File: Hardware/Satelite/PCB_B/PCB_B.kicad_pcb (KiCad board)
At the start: 2 copper layers, 54 x 54 mm, 92 parts, among them IC1 MCP1642B-50I_MS, IC2 MCP1642B-50I_MS, J1 Conector_PCB_B-C, J2 Conector_PCB_A-B, M1 Spacer, M2 Spacer, M3 Spacer, Q1 SSM3J338R,LF, Q2 SSM3J338R,LF, Q3 SSM3J338R,LF, U1 MIC5353-3.3YMT, U10 BQ21040DBVR, U2 ADP2108AUJ-3.3, U3 INA194, U4 MCP6001-OT, U5 INA194, U6 MCP6001-OT, U7 INA216A4RSWR, U8 BQ27441DRZR-G1A, U9 MCP6001-OT

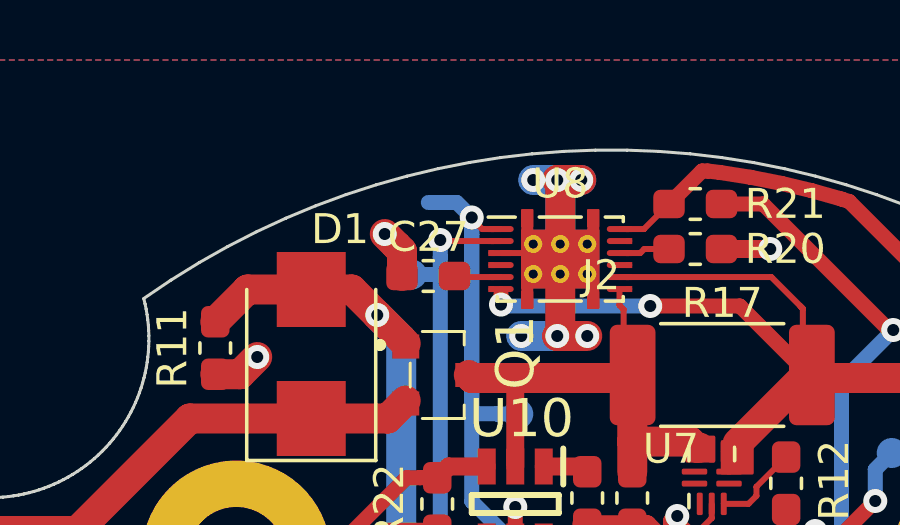
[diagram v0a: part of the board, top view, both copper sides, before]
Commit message: PCB_B plano de masa mejorado
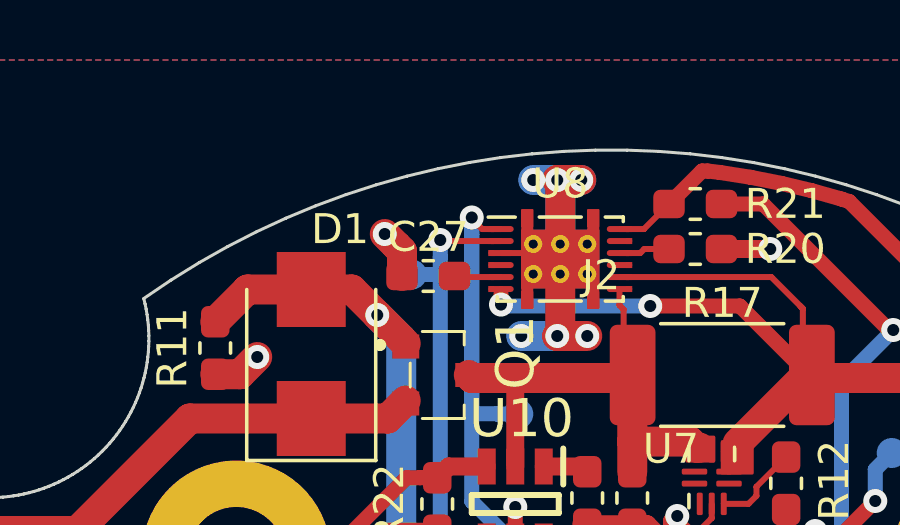
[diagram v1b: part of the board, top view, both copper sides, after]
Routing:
- net /SDA: track 59.2 -> 57.5 mm
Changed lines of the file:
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@@
     (thickness 1.6)
     (drawings 21)
-    (tracks 854)
+    (tracks 852)
     (zones 0)
     (modules 92)
@@
   (segment (start -4.625 13.5964) (end -5.1 13.5964) (width 0.6) (layer B.Cu) (net 3) (status 30))
   (segment (start -5.1 13.5964) (end -6.3 12.3964) (width 0.6) (layer B.Cu) (net 3) (status 10))
+  (segment (start 13.35 -5.205) (end 13.35 -4.73) (width 0.2) (layer F.Cu) (net 3) (status 10))
+  (segment (start 12.599999 -4.399995) (end 12.2 -4.799994) (width 0.2) (layer F.Cu) (net 3))
+  (segment (start 13.019995 -4.399995) (end 12.599999 -4.399995) (width 0.2) (layer F.Cu) (net 3))
+  (segment (start 13.35 -4.73) (end 13.019995 -4.399995) (width 0.2) (layer F.Cu) (net 3))
+  (segment (start 8.200018 -10.8) (end 9.2 -10.8) (width 1) (layer F.Cu) (net 3))
+  (segment (start 7 -10.8) (end 8.200018 -10.8) (width 1) (layer B.Cu) (net 3))
+  (via (at 7.4 -16) (size 0.8) (drill 0.4) (layers F.Cu B.Cu) (net 3))
+  (segment (start 9 -16) (end 7.4 -16) (width 1) (layer B.Cu) (net 3))
+  (via (at 0.11 15.07) (size 0.8) (drill 0.4) (layers F.Cu B.Cu) (net 3))
+  (segment (start 1.3 15.075) (end 0.115 15.075) (width 1) (layer F.Cu) (net 3))
+  (segment (start 0.115 15.075) (end 0.11 15.07) (width 1) (layer F.Cu) (net 3))
+  (segment (start -0.695 14.265) (end 0.11 15.07) (width 1) (layer F.Cu) (net 3))
+  (segment (start -0.695 13.13) (end -0.695 14.265) (width 1) (layer F.Cu) (net 3))
   (segment (start 4.575 -6.45) (end 4.2 -6.075) (width 0.6) (layer F.Cu) (net 4) (status 30))
   (segment (start 5.85 -6.45) (end 4.575 -6.45) (width 0.6) (layer F.Cu) (net 4) (status 30))
@@
   (segment (start -7.81 5.565001) (end -7.825 5.550001) (width 1) (layer F.Cu) (net 5))
   (segment (start -7.81 6.19) (end -7.81 5.565001) (width 1) (layer F.Cu) (net 5))
+  (segment (start 2.67 13.13) (end 2.9 13.36) (width 1) (layer F.Cu) (net 5))
+  (segment (start 1.355 13.13) (end 2.67 13.13) (width 1) (layer F.Cu) (net 5))
+  (segment (start 2.9 12.75) (end 2.9 13.36) (width 1) (layer F.Cu) (net 5))
+  (segment (start 2.9 13.36) (end 2.9 16.2) (width 1) (layer F.Cu) (net 5))
   (segment (start -4.625 11.1964) (end -0.825 11.1964) (width 0.5) (layer B.Cu) (net 6) (status 30))
   (segment (start 18.025 22.925) (end 18.6 22.925) (width 1) (layer F.Cu) (net 6) (status 20))
@@
   (segment (start 11.3 -11.8) (end 6.37251 -11.8) (width 0.5) (layer B.Cu) (net 10))
   (segment (start 16.3875 -9.4) (end 14.212501 -7.225001) (width 1) (layer F.Cu) (net 10) (status 10))
+  (segment (start 13.925 -6.78) (end 13.75 -6.955) (width 0.2) (layer F.Cu) (net 10) (status 20))
+  (segment (start 13.925 -6.28) (end 13.925 -6.78) (width 0.2) (layer F.Cu) (net 10) (status 10))
   (segment (start 23.675 18.8) (end 24.2 18.275) (width 0.5) (layer F.Cu) (net 11) (status 20))
   (segment (start 22.475 18.8) (end 23.675 18.8) (width 0.5) (layer F.Cu) (net 11) (status 10))
@@
   (segment (start -9.2 7.29) (end -9.2 7.855685) (width 0.5) (layer F.Cu) (net 19))
   (segment (start -9.2 7.855685) (end -12.450001 11.105686) (width 0.5) (layer F.Cu) (net 19))
+  (via (at 16.9 -1.07) (size 0.8) (drill 0.4) (layers F.Cu B.Cu) (net 19))
+  (segment (start 16.925 -1.1) (end 16.9 -1.075) (width 0.5) (layer F.Cu) (net 19))
+  (segment (start 19.4 -11) (end 17.675 -9.275) (width 0.5) (layer B.Cu) (net 19))
+  (segment (start 17.299999 -1.469999) (end 16.9 -1.07) (width 0.5) (layer B.Cu) (net 19))
+  (segment (start 17.675 -9.275) (end 17.675 -1.845) (width 0.5) (layer B.Cu) (net 19))
+  (segment (start 17.675 -1.845) (end 17.299999 -1.469999) (width 0.5) (layer B.Cu) (net 19))
+  (segment (start 16.9 -1.075) (end 16.9 -1.07) (width 0.5) (layer F.Cu) (net 19))
+  (segment (start 17.75 -1.1) (end 16.925 -1.1) (width 0.5) (layer F.Cu) (net 19))
+  (segment (start 17.675 -1.025) (end 17.75 -1.1) (width 0.5) (layer F.Cu) (net 19))
+  (segment (start 17.675 2.4) (end 17.675 -1.025) (width 0.5) (layer F.Cu) (net 19))
   (segment (start 27.19001 14.51001) (end 17.152008 14.51001) (width 0.5) (layer F.Cu) (net 20))
   (segment (start 27.95 16.3) (end 27.95 15.27) (width 0.5) (layer F.Cu) (net 20) (status 10))
@@
   (segment (start 11.791998 1.15) (end 5.35 -5.291998) (width 0.5) (layer B.Cu) (net 25))
   (segment (start 21.2 1.15) (end 11.791998 1.15) (width 0.5) (layer B.Cu) (net 25))
-  (segment (start 4.85 -15.25) (end 5.35 -14.75) (width 0.5) (layer B.Cu) (net 25))
-  (segment (start 3.9 -15.25) (end 4.85 -15.25) (width 0.5) (layer B.Cu) (net 25))
   (segment (start 6.184892 -8.208002) (end 5.35 -8.208002) (width 0.5) (layer B.Cu) (net 25))
   (segment (start 6.192894 -8.2) (end 6.184892 -8.208002) (width 0.5) (layer B.Cu) (net 25))
@@
   (segment (start 10.4125 -9.4) (end 7 -9.4) (width 1) (layer F.Cu) (net 47) (status 10))
   (segment (start 7 -9.4) (end 5.35 -9.4) (width 1) (layer F.Cu) (net 47) (status 20))
+  (segment (start 10.7 -9.4875) (end 10.7125 -9.5) (width 1) (layer F.Cu) (net 47))
+  (segment (start 12.82499 -7.08001) (end 12.94999 -7.08001) (width 1) (layer F.Cu) (net 47))
+  (segment (start 12.625 -7.28) (end 12.82499 -7.08001) (width 1) (layer F.Cu) (net 47))
+  (segment (start 10.7 -7.28) (end 12.625 -7.28) (width 1) (layer F.Cu) (net 47))
+  (segment (start 10.7 -7.28) (end 10.7 -9.4875) (width 1) (layer F.Cu) (net 47))
+  (segment (start 10.7 -6.275) (end 10.7 -7.28) (width 1) (layer F.Cu) (net 47))
   (segment (start -12.267738 -1.500841) (end -12.267738 -2.732262) (width 1) (layer F.Cu) (net 48) (status 10))
   (segment (start -12.267738 -2.732262) (end -10.7 -4.3) (width 1) (layer F.Cu) (net 48))
@@
   (segment (start -0.6 20.4) (end -0.2 20.8) (width 0.5) (layer F.Cu) (net 50))
   (segment (start 0.6 22.725) (end 0.6 20.8) (width 0.5) (layer F.Cu) (net 50) (status 30))
-  (segment (start 13.35 -5.205) (end 13.35 -4.73) (width 0.2) (layer F.Cu) (net 3) (status 10))
-  (segment (start 12.599999 -4.399995) (end 12.2 -4.799994) (width 0.2) (layer F.Cu) (net 3))
-  (segment (start 13.019995 -4.399995) (end 12.599999 -4.399995) (width 0.2) (layer F.Cu) (net 3))
-  (segment (start 13.35 -4.73) (end 13.019995 -4.399995) (width 0.2) (layer F.Cu) (net 3))
-  (segment (start 8.200018 -10.8) (end 9.2 -10.8) (width 1) (layer F.Cu) (net 3))
-  (segment (start 7 -10.8) (end 8.200018 -10.8) (width 1) (layer B.Cu) (net 3))
-  (via (at 7.4 -16) (size 0.8) (drill 0.4) (layers F.Cu B.Cu) (net 3))
-  (segment (start 9 -16) (end 7.4 -16) (width 1) (layer B.Cu) (net 3))
-  (via (at 0.11 15.07) (size 0.8) (drill 0.4) (layers F.Cu B.Cu) (net 3))
-  (segment (start 1.3 15.075) (end 0.115 15.075) (width 1) (layer F.Cu) (net 3))
-  (segment (start 0.115 15.075) (end 0.11 15.07) (width 1) (layer F.Cu) (net 3))
-  (segment (start -0.695 14.265) (end 0.11 15.07) (width 1) (layer F.Cu) (net 3))
-  (segment (start -0.695 13.13) (end -0.695 14.265) (width 1) (layer F.Cu) (net 3))
-  (segment (start 2.67 13.13) (end 2.9 13.36) (width 1) (layer F.Cu) (net 5))
-  (segment (start 1.355 13.13) (end 2.67 13.13) (width 1) (layer F.Cu) (net 5))
-  (segment (start 2.9 12.75) (end 2.9 13.36) (width 1) (layer F.Cu) (net 5))
-  (segment (start 2.9 13.36) (end 2.9 16.2) (width 1) (layer F.Cu) (net 5))
-  (segment (start 13.925 -6.78) (end 13.75 -6.955) (width 0.2) (layer F.Cu) (net 10) (status 20))
-  (segment (start 13.925 -6.28) (end 13.925 -6.78) (width 0.2) (layer F.Cu) (net 10) (status 10))
-  (via (at 16.9 -1.07) (size 0.8) (drill 0.4) (layers F.Cu B.Cu) (net 19))
-  (segment (start 16.925 -1.1) (end 16.9 -1.075) (width 0.5) (layer F.Cu) (net 19))
-  (segment (start 19.4 -11) (end 17.675 -9.275) (width 0.5) (layer B.Cu) (net 19))
-  (segment (start 17.299999 -1.469999) (end 16.9 -1.07) (width 0.5) (layer B.Cu) (net 19))
-  (segment (start 17.675 -9.275) (end 17.675 -1.845) (width 0.5) (layer B.Cu) (net 19))
-  (segment (start 17.675 -1.845) (end 17.299999 -1.469999) (width 0.5) (layer B.Cu) (net 19))
-  (segment (start 16.9 -1.075) (end 16.9 -1.07) (width 0.5) (layer F.Cu) (net 19))
-  (segment (start 17.75 -1.1) (end 16.925 -1.1) (width 0.5) (layer F.Cu) (net 19))
-  (segment (start 17.675 -1.025) (end 17.75 -1.1) (width 0.5) (layer F.Cu) (net 19))
-  (segment (start 17.675 2.4) (end 17.675 -1.025) (width 0.5) (layer F.Cu) (net 19))
-  (segment (start 10.7 -9.4875) (end 10.7125 -9.5) (width 1) (layer F.Cu) (net 47))
-  (segment (start 12.82499 -7.08001) (end 12.94999 -7.08001) (width 1) (layer F.Cu) (net 47))
-  (segment (start 12.625 -7.28) (end 12.82499 -7.08001) (width 1) (layer F.Cu) (net 47))
-  (segment (start 10.7 -7.28) (end 12.625 -7.28) (width 1) (layer F.Cu) (net 47))
-  (segment (start 10.7 -7.28) (end 10.7 -9.4875) (width 1) (layer F.Cu) (net 47))
-  (segment (start 10.7 -6.275) (end 10.7 -7.28) (width 1) (layer F.Cu) (net 47))
   (segment (start 13.75 -5.205) (end 14.575 -5.205) (width 0.2) (layer F.Cu) (net 51))
   (segment (start 14.575 -5.205) (end 14.84 -5.47) (width 0.2) (layer F.Cu) (net 51))

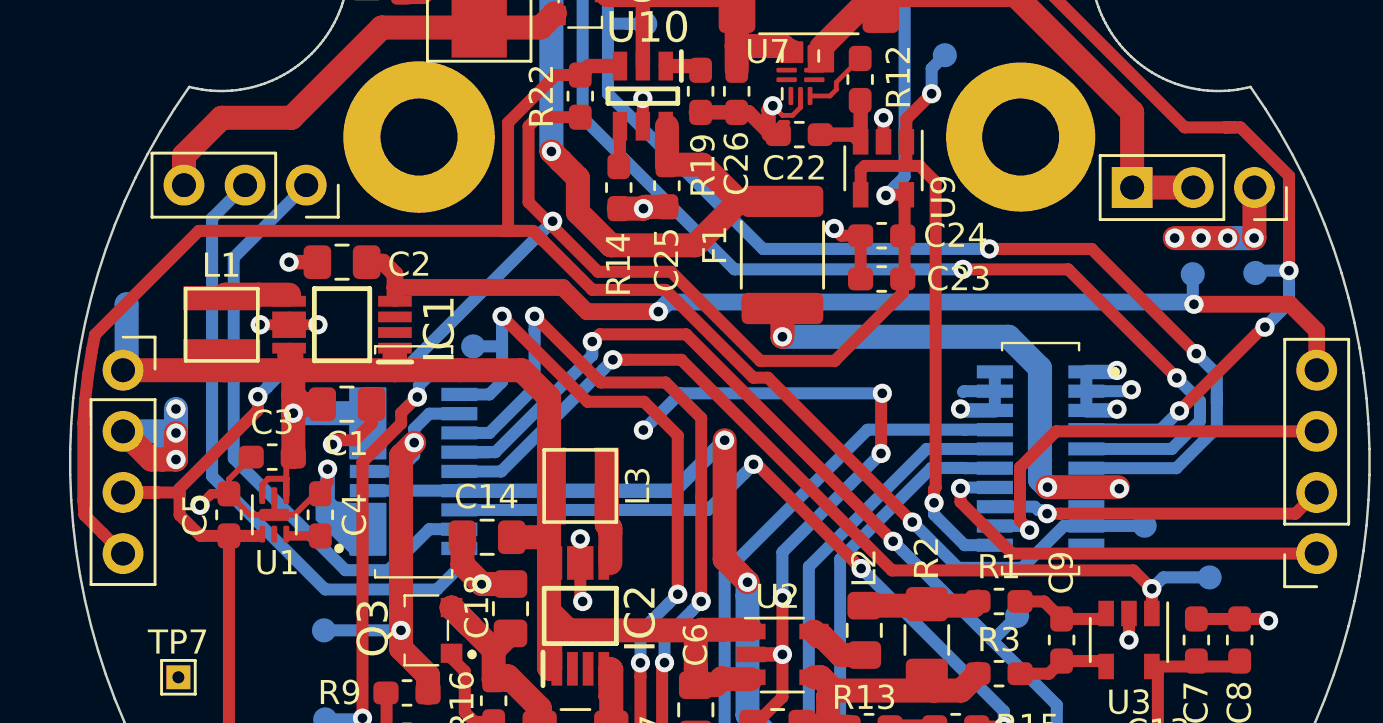
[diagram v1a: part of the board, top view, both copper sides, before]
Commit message: Correcciones en conector B-C lado B
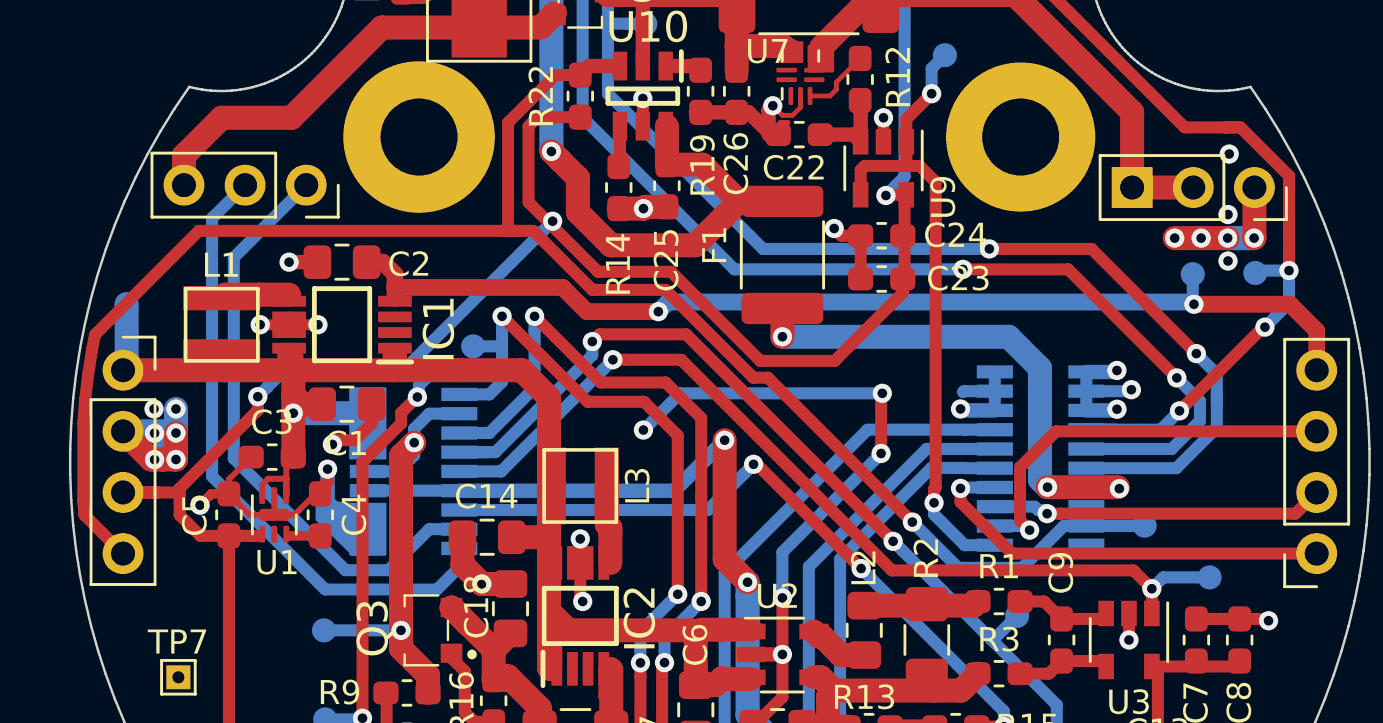
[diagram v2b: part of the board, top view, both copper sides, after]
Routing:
- net GND: vias 49 -> 55

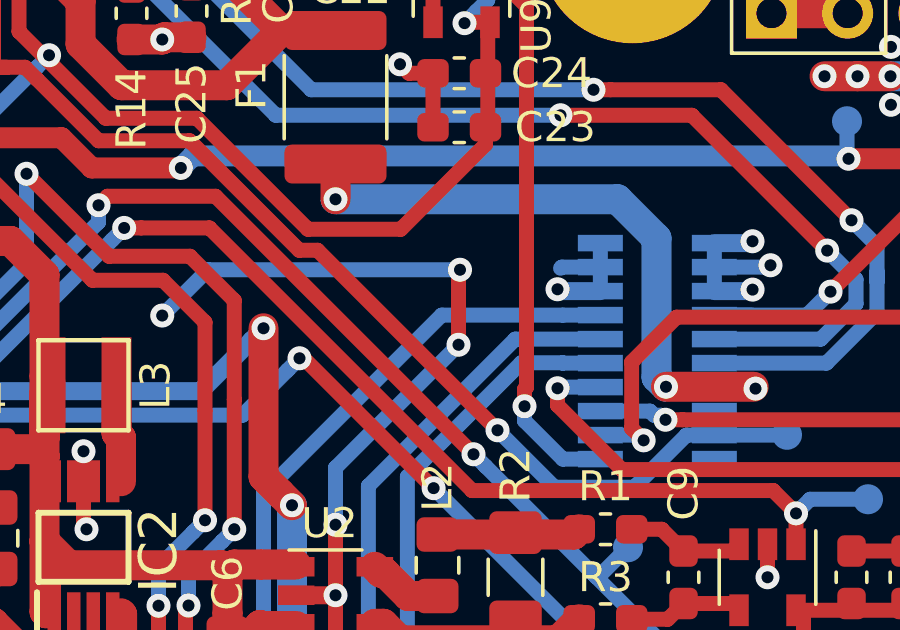
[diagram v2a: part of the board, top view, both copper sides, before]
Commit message: Agregado de logos faltantes en PCB_B
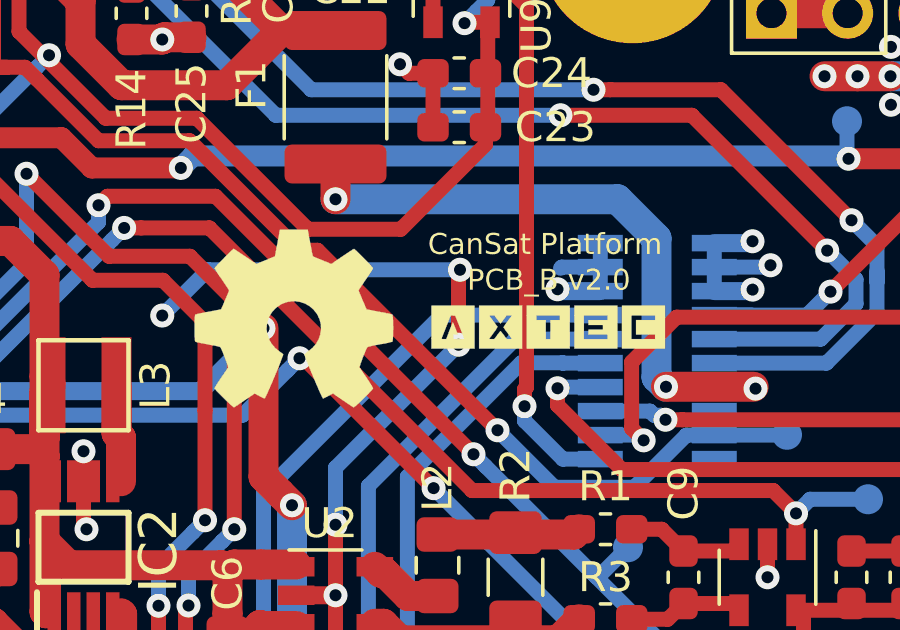
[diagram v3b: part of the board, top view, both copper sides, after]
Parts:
- added G***: LOGO, AXTEC:Logo_AXTEC, B.Cu at (11.8, 8.38)
- added G***: LOGO, AXTEC:Logo_AXTEC, F.Cu at (19.8, 8.86)
- added REF**: OSHW-Symbol_6.7x6mm_SilkScreen, Symbol:OSHW-Symbol_6.7x6mm_SilkScreen, B.Cu at (12.0, 13.4)
- added REF**: OSHW-Symbol_6.7x6mm_SilkScreen, Symbol:OSHW-Symbol_6.7x6mm_SilkScreen, F.Cu at (11.2, 8.79)
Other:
- board text added: "CanSat Platform"
- board text added: "PCB_B v2.0"

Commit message: Nuevos gerbers generados para todos los PCB
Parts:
- moved TP14 2.90 mm to (35.0, 3.20)
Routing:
- net GND: track 149.0 -> 130.3 mm, vias 55 -> 70
- net +3V3_Internal: track 159.5 -> 162.7 mm
- net /GPOUT: track 48.8 -> 50.6 mm
- net /ENABLE_5V: track 41.6 -> 40.2 mm
- net /ENABLE_3V3: track 29.4 -> 30.7 mm
- net /P1: track 24.6 -> 25.7 mm
- net /I_SENSE_5V: track 39.0 -> 38.0 mm
